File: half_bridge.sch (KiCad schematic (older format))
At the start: 9 parts, among them Q11 MOSFET_N, Q12 MOSFET_N, U6 IR2184

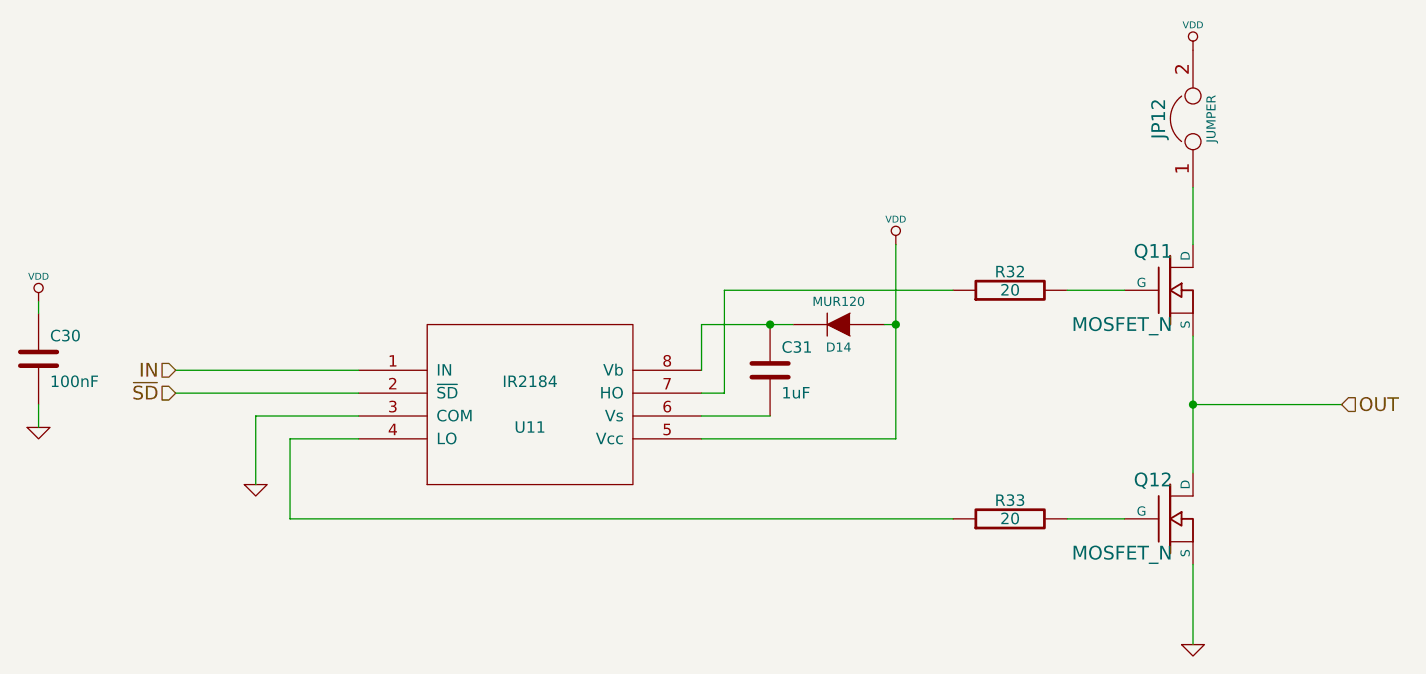
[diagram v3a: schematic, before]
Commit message: fixed gnd/vcc flips
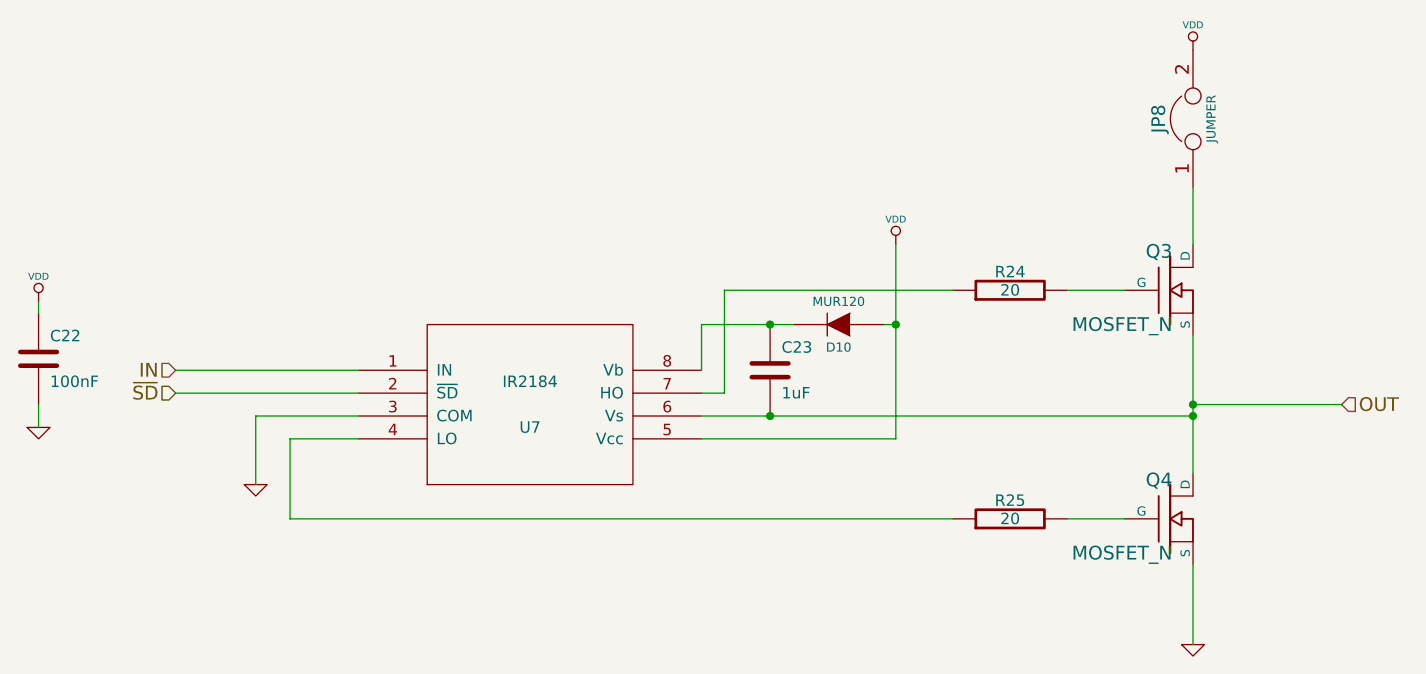
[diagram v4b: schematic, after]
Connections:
- net OUT: now also C31.2, U6.6 (Vs)
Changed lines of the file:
@@
-EESchema Schematic File Version 2  date Thu 09 Jan 2014 04:30:17 AM EST
+EESchema Schematic File Version 2
 LIBS:power
 LIBS:device
@@
 LIBS:STM32L100xx_LQFP64
 LIBS:IR2184
-LIBS:-cache
 LIBS:LM25011
 LIBS:open-project
 LIBS:hackboard-cache
-EELAYER 25  0
+EELAYER 24 0
 EELAYER END
-$Descr A4 11700 8267
+$Descr A4 11693 8268
 encoding utf-8
-Sheet 4 7
+Sheet 3 7
 Title "noname.sch"
 Date "9 jan 2014"
@@
 AR Path="/52783943/52BF660C" Ref="#PWR094"  Part="1"
 AR Path="/5278392A/52BF660C" Ref="#PWR0100"  Part="1"
-F 0 "#PWR0100" H 2500 2500 30  0001 C CNN
+F 0 "#PWR076" H 2500 2500 30  0001 C CNN
 F 1 "VDD" H 2500 2510 30  0000 C CNN
+F 2 "" H 2500 2400 60  0001 C CNN
+F 3 "" H 2500 2400 60  0001 C CNN
 	1    2500 2400
 	1    0    0    -1
@@
 AR Path="/52783943/52BF650C" Ref="#PWR095"  Part="1"
 AR Path="/5278392A/52BF650C" Ref="#PWR0101"  Part="1"
-F 0 "#PWR0101" H 6250 2250 30  0001 C CNN
+F 0 "#PWR077" H 6250 2250 30  0001 C CNN
 F 1 "VDD" H 6250 2260 30  0000 C CNN
+F 2 "" H 6250 2150 60  0001 C CNN
+F 3 "" H 6250 2150 60  0001 C CNN
 	1    6250 2150
 	1    0    0    -1
@@
 	3100 2700 3900 2700
 Wire Wire Line
-	5700 2900 5400 2900
+	5400 2900 7550 2900
 Wire Wire Line
 	6250 2500 6200 2500
@@
 AR Path="/52783943/527843FF" Ref="#PWR096"  Part="1"
 AR Path="/5278392A/527843FF" Ref="#PWR0102"  Part="1"
-F 0 "#PWR0102" H 2500 2950 30  0001 C CNN
+F 0 "#PWR078" H 2500 2950 30  0001 C CNN
 F 1 "GND" H 2500 2880 30  0001 C CNN
+F 2 "" H 2500 2950 60  0001 C CNN
+F 3 "" H 2500 2950 60  0001 C CNN
 	1    2500 2950
 	1    0    0    -1
@@
 AR Path="/52783943/527843E9" Ref="C28"  Part="1"
 AR Path="/5278392A/527843E9" Ref="C30"  Part="1"
-F 0 "C30" H 2550 2750 50  0000 L CNN
+F 0 "C22" H 2550 2750 50  0000 L CNN
 F 1 "100nF" H 2550 2550 50  0000 L CNN
+F 2 "" H 2500 2650 60  0001 C CNN
+F 3 "" H 2500 2650 60  0001 C CNN
 	1    2500 2650
 	1    0    0    -1
@@
 AR Path="/52783E34/527838B2" Ref="R29"  Part="1"
 AR Path="/52783943/527838B2" Ref="R31"  Part="1"
-F 0 "R33" V 6830 3350 50  0000 C CNN
+F 0 "R25" V 6830 3350 50  0000 C CNN
 F 1 "20" V 6750 3350 50  0000 C CNN
+F 2 "" H 6750 3350 60  0001 C CNN
+F 3 "" H 6750 3350 60  0001 C CNN
 	1    6750 3350
 	0    -1   -1   0
@@
 AR Path="/52783E34/5278387F" Ref="R28"  Part="1"
 AR Path="/52783943/5278387F" Ref="R30"  Part="1"
-F 0 "R32" V 6830 2350 50  0000 C CNN
+F 0 "R24" V 6830 2350 50  0000 C CNN
 F 1 "20" V 6750 2350 50  0000 C CNN
+F 2 "" H 6750 2350 60  0001 C CNN
+F 3 "" H 6750 2350 60  0001 C CNN
 	1    6750 2350
 	0    -1   -1   0
@@
 AR Path="/52783943/5278382D" Ref="U10"  Part="1"
 AR Path="/5278392A/5278382D" Ref="U11"  Part="1"
-F 0 "U11" H 4650 2750 50  0000 C CNN
+F 0 "U7" H 4650 2750 50  0000 C CNN
 F 1 "IR2184" H 4650 2950 50  0000 C CNN
 F 2 "MODULE" H 4650 2850 50  0001 C CNN
@@
 AR Path="/52783E34/52783639" Ref="#PWR091"  Part="1"
 AR Path="/52783943/52783639" Ref="#PWR097"  Part="1"
-F 0 "#PWR0103" H 3450 3200 30  0001 C CNN
+F 0 "#PWR079" H 3450 3200 30  0001 C CNN
 F 1 "GND" H 3450 3130 30  0001 C CNN
+F 2 "" H 3450 3200 60  0001 C CNN
+F 3 "" H 3450 3200 60  0001 C CNN
 	1    3450 3200
 	1    0    0    -1
@@
 AR Path="/52783E34/527835B9" Ref="C27"  Part="1"
 AR Path="/52783943/527835B9" Ref="C29"  Part="1"
-F 0 "C31" H 5750 2800 50  0000 L CNN
+F 0 "C23" H 5750 2800 50  0000 L CNN
 F 1 "1uF" H 5750 2600 50  0000 L CNN
+F 2 "" H 5700 2700 60  0001 C CNN
+F 3 "" H 5700 2700 60  0001 C CNN
 	1    5700 2700
 	1    0    0    -1
@@
 AR Path="/52783E34/5278358E" Ref="D12"  Part="1"
 AR Path="/52783943/5278358E" Ref="D13"  Part="1"
-F 0 "D14" H 6000 2600 40  0000 C CNN
+F 0 "D10" H 6000 2600 40  0000 C CNN
 F 1 "MUR120" H 6000 2400 40  0000 C CNN
+F 2 "" H 6000 2500 60  0001 C CNN
+F 3 "" H 6000 2500 60  0001 C CNN
 	1    6000 2500
 	-1   0    0    1
@@
 AR Path="/52783E34/52783118" Ref="JP10"  Part="1"
 AR Path="/52783943/52783118" Ref="JP11"  Part="1"
-F 0 "JP12" H 7550 1750 60  0000 C CNN
+F 0 "JP8" H 7550 1750 60  0000 C CNN
 F 1 "JUMPER" H 7550 1520 40  0000 C CNN
+F 2 "" H 7550 1600 60  0001 C CNN
+F 3 "" H 7550 1600 60  0001 C CNN
 	1    7550 1600
 	0    -1   -1   0
@@
 AR Path="/52783E34/52783104" Ref="#PWR092"  Part="1"
 AR Path="/52783943/52783104" Ref="#PWR098"  Part="1"
-F 0 "#PWR0104" H 7550 3900 30  0001 C CNN
+F 0 "#PWR080" H 7550 3900 30  0001 C CNN
 F 1 "GND" H 7550 3830 30  0001 C CNN
+F 2 "" H 7550 3900 60  0001 C CNN
+F 3 "" H 7550 3900 60  0001 C CNN
 	1    7550 3900
 	1    0    0    -1
@@
 AR Path="/52783E34/527830FD" Ref="#PWR093"  Part="1"
 AR Path="/52783943/527830FD" Ref="#PWR099"  Part="1"
-F 0 "#PWR0105" H 7550 1400 30  0001 C CNN
+F 0 "#PWR081" H 7550 1400 30  0001 C CNN
 F 1 "VDD" H 7550 1410 30  0000 C CNN
+F 2 "" H 7550 1300 60  0001 C CNN
+F 3 "" H 7550 1300 60  0001 C CNN
 	1    7550 1300
 	1    0    0    -1
@@
 AR Path="/52783E34/527830EC" Ref="Q8"  Part="1"
 AR Path="/52783943/527830EC" Ref="Q10"  Part="1"
-F 0 "Q12" H 7460 3520 60  0000 R CNN
+F 0 "Q4" H 7460 3520 60  0000 R CNN
 F 1 "MOSFET_N" H 7460 3200 60  0000 R CNN
+F 2 "" H 7450 3350 60  0001 C CNN
+F 3 "" H 7450 3350 60  0001 C CNN
 	1    7450 3350
 	1    0    0    -1
@@
 AR Path="/52783E34/527830DE" Ref="Q7"  Part="1"
 AR Path="/52783943/527830DE" Ref="Q9"  Part="1"
-F 0 "Q11" H 7460 2520 60  0000 R CNN
+F 0 "Q3" H 7460 2520 60  0000 R CNN
 F 1 "MOSFET_N" H 7460 2200 60  0000 R CNN
+F 2 "" H 7450 2350 60  0001 C CNN
+F 3 "" H 7450 2350 60  0001 C CNN
 	1    7450 2350
 	1    0    0    -1
 $EndComp
+Connection ~ 5700 2900
+Connection ~ 7550 2900
 $EndSCHEMATC

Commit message: didn't save everyting
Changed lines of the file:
@@
 AR Path="/52783943/52BF660C" Ref="#PWR094"  Part="1"
 AR Path="/5278392A/52BF660C" Ref="#PWR0100"  Part="1"
-F 0 "#PWR076" H 2500 2500 30  0001 C CNN
+F 0 "#PWR0100" H 2500 2500 30  0001 C CNN
 F 1 "VDD" H 2500 2510 30  0000 C CNN
 F 2 "" H 2500 2400 60  0001 C CNN
@@
 AR Path="/52783943/52BF650C" Ref="#PWR095"  Part="1"
 AR Path="/5278392A/52BF650C" Ref="#PWR0101"  Part="1"
-F 0 "#PWR077" H 6250 2250 30  0001 C CNN
+F 0 "#PWR0101" H 6250 2250 30  0001 C CNN
 F 1 "VDD" H 6250 2260 30  0000 C CNN
 F 2 "" H 6250 2150 60  0001 C CNN
@@
 AR Path="/52783943/527843FF" Ref="#PWR096"  Part="1"
 AR Path="/5278392A/527843FF" Ref="#PWR0102"  Part="1"
-F 0 "#PWR078" H 2500 2950 30  0001 C CNN
+F 0 "#PWR0102" H 2500 2950 30  0001 C CNN
 F 1 "GND" H 2500 2880 30  0001 C CNN
 F 2 "" H 2500 2950 60  0001 C CNN
@@
 AR Path="/52783943/527843E9" Ref="C28"  Part="1"
 AR Path="/5278392A/527843E9" Ref="C30"  Part="1"
-F 0 "C22" H 2550 2750 50  0000 L CNN
+F 0 "C30" H 2550 2750 50  0000 L CNN
 F 1 "100nF" H 2550 2550 50  0000 L CNN
 F 2 "" H 2500 2650 60  0001 C CNN
@@
 AR Path="/52783E34/527838B2" Ref="R29"  Part="1"
 AR Path="/52783943/527838B2" Ref="R31"  Part="1"
-F 0 "R25" V 6830 3350 50  0000 C CNN
+F 0 "R33" V 6830 3350 50  0000 C CNN
 F 1 "20" V 6750 3350 50  0000 C CNN
 F 2 "" H 6750 3350 60  0001 C CNN
@@
 AR Path="/52783E34/5278387F" Ref="R28"  Part="1"
 AR Path="/52783943/5278387F" Ref="R30"  Part="1"
-F 0 "R24" V 6830 2350 50  0000 C CNN
+F 0 "R32" V 6830 2350 50  0000 C CNN
 F 1 "20" V 6750 2350 50  0000 C CNN
 F 2 "" H 6750 2350 60  0001 C CNN
@@
 AR Path="/52783943/5278382D" Ref="U10"  Part="1"
 AR Path="/5278392A/5278382D" Ref="U11"  Part="1"
-F 0 "U7" H 4650 2750 50  0000 C CNN
+F 0 "U11" H 4650 2750 50  0000 C CNN
 F 1 "IR2184" H 4650 2950 50  0000 C CNN
 F 2 "MODULE" H 4650 2850 50  0001 C CNN
@@
 AR Path="/52783E34/52783639" Ref="#PWR091"  Part="1"
 AR Path="/52783943/52783639" Ref="#PWR097"  Part="1"
-F 0 "#PWR079" H 3450 3200 30  0001 C CNN
+F 0 "#PWR0103" H 3450 3200 30  0001 C CNN
 F 1 "GND" H 3450 3130 30  0001 C CNN
 F 2 "" H 3450 3200 60  0001 C CNN
@@
 AR Path="/52783E34/527835B9" Ref="C27"  Part="1"
 AR Path="/52783943/527835B9" Ref="C29"  Part="1"
-F 0 "C23" H 5750 2800 50  0000 L CNN
+F 0 "C31" H 5750 2800 50  0000 L CNN
 F 1 "1uF" H 5750 2600 50  0000 L CNN
 F 2 "" H 5700 2700 60  0001 C CNN
@@
 AR Path="/52783E34/5278358E" Ref="D12"  Part="1"
 AR Path="/52783943/5278358E" Ref="D13"  Part="1"
-F 0 "D10" H 6000 2600 40  0000 C CNN
+F 0 "D14" H 6000 2600 40  0000 C CNN
 F 1 "MUR120" H 6000 2400 40  0000 C CNN
 F 2 "" H 6000 2500 60  0001 C CNN
@@
 AR Path="/52783E34/52783118" Ref="JP10"  Part="1"
 AR Path="/52783943/52783118" Ref="JP11"  Part="1"
-F 0 "JP8" H 7550 1750 60  0000 C CNN
+F 0 "JP12" H 7550 1750 60  0000 C CNN
 F 1 "JUMPER" H 7550 1520 40  0000 C CNN
 F 2 "" H 7550 1600 60  0001 C CNN
@@
 AR Path="/52783E34/52783104" Ref="#PWR092"  Part="1"
 AR Path="/52783943/52783104" Ref="#PWR098"  Part="1"
-F 0 "#PWR080" H 7550 3900 30  0001 C CNN
+F 0 "#PWR0104" H 7550 3900 30  0001 C CNN
 F 1 "GND" H 7550 3830 30  0001 C CNN
 F 2 "" H 7550 3900 60  0001 C CNN
@@
 AR Path="/52783E34/527830FD" Ref="#PWR093"  Part="1"
 AR Path="/52783943/527830FD" Ref="#PWR099"  Part="1"
-F 0 "#PWR081" H 7550 1400 30  0001 C CNN
+F 0 "#PWR0105" H 7550 1400 30  0001 C CNN
 F 1 "VDD" H 7550 1410 30  0000 C CNN
 F 2 "" H 7550 1300 60  0001 C CNN
@@
 AR Path="/52783E34/527830EC" Ref="Q8"  Part="1"
 AR Path="/52783943/527830EC" Ref="Q10"  Part="1"
-F 0 "Q4" H 7460 3520 60  0000 R CNN
+F 0 "Q12" H 7460 3520 60  0000 R CNN
 F 1 "MOSFET_N" H 7460 3200 60  0000 R CNN
 F 2 "" H 7450 3350 60  0001 C CNN
@@
 AR Path="/52783E34/527830DE" Ref="Q7"  Part="1"
 AR Path="/52783943/527830DE" Ref="Q9"  Part="1"
-F 0 "Q3" H 7460 2520 60  0000 R CNN
+F 0 "Q11" H 7460 2520 60  0000 R CNN
 F 1 "MOSFET_N" H 7460 2200 60  0000 R CNN
 F 2 "" H 7450 2350 60  0001 C CNN
